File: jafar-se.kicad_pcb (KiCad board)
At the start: 2 copper layers, 33 x 41 mm, 16 parts, among them J1 XBOX LPC, J2 JTAG, J3 D0, J4 PLCC-32 Socket, U1 LC4032V-75TN44I

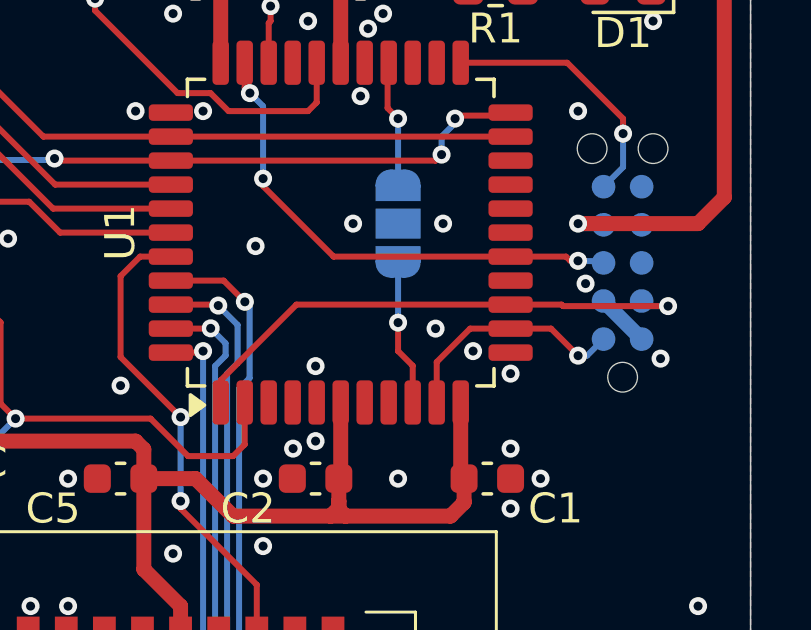
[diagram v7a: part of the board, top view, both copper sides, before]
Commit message: Reroute jtag to not go through CPLD pins
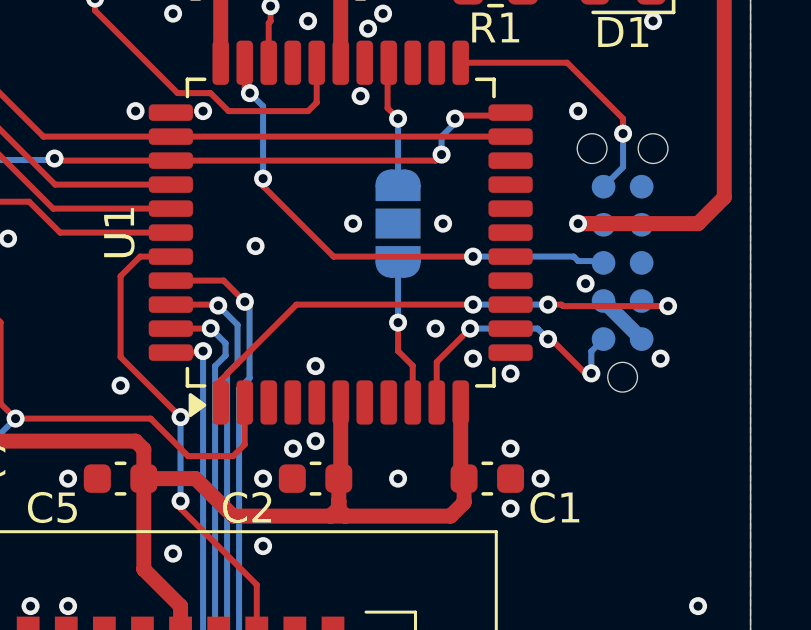
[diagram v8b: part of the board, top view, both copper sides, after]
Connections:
- U1 pad 13: /TCK -> unconnected-(U1-A12-Pad13)
- U1 pad 14: /TDI -> unconnected-(U1-A13-Pad14)
- U1 pad 16: /TDO -> unconnected-(U1-A15-Pad16)
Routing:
- net /TCK: track 7.97 -> 8.89 mm, vias 1 -> 3
- net /TDI: vias 1 -> 3
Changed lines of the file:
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@@
 			(layers "F.Cu" "F.Mask" "F.Paste")
 			(roundrect_rratio 0.25)
-			(net "/TCK")
+			(net "unconnected-(U1-A12-Pad13)")
 			(pinfunction "A12_13")
-			(pintype "bidirectional")
+			(pintype "bidirectional+no_connect")
 		)
 		(pad "14" smd roundrect
@@
 			(layers "F.Cu" "F.Mask" "F.Paste")
 			(roundrect_rratio 0.25)
-			(net "/TDI")
+			(net "unconnected-(U1-A13-Pad14)")
 			(pinfunction "A13_14")
-			(pintype "bidirectional")
+			(pintype "bidirectional+no_connect")
 		)
 		(pad "15" smd roundrect
@@
 			(layers "F.Cu" "F.Mask" "F.Paste")
 			(roundrect_rratio 0.25)
-			(net "/TDO")
+			(net "unconnected-(U1-A15-Pad16)")
 			(pinfunction "A15_16")
-			(pintype "bidirectional")
+			(pintype "bidirectional+no_connect")
 		)
 		(pad "17" smd roundrect
@@
 	)
 	(via
-		(at 143.75 61.75)
+		(at 143.75 62)
 		(size 0.6)
 		(drill 0.3)
@@
 	(segment
 		(start 137.862501 60.2)
-		(end 145 60.2)
+		(end 143.75 60.2)
 		(width 0.2)
 		(layer "F.Cu")
@@
 	)
 	(segment
-		(start 145 60.2)
-		(end 146.7 60.2)
+		(start 135.3375 63.4625)
+		(end 135.3375 62.725001)
 		(width 0.2)
 		(layer "F.Cu")
@@
 	)
 	(segment
-		(start 135.3375 63.4625)
-		(end 135.3375 62.725001)
+		(start 146.25 60.2)
+		(end 146.7 60.2)
 		(width 0.2)
 		(layer "F.Cu")
@@
 	)
 	(via
+		(at 146.25 60.2)
+		(size 0.6)
+		(drill 0.3)
+		(layers "F.Cu" "B.Cu")
+		(net "/TDI")
+	)
+	(via
+		(at 143.75 60.2)
+		(size 0.6)
+		(drill 0.3)
+		(layers "F.Cu" "B.Cu")
+		(net "/TDI")
+	)
+	(via
 		(at 150.25 60.25)
 		(size 0.6)
@@
 	)
 	(segment
+		(start 143.75 60.2)
+		(end 146.25 60.2)
+		(width 0.2)
+		(layer "B.Cu")
+		(net "/TDI")
+	)
+	(segment
 		(start 141.75 63.45)
 		(end 141.7375 63.4625)
@@
 	)
 	(segment
-		(start 143.651471 61)
-		(end 145 61)
+		(start 147.692416 62.492978)
+		(end 147.492978 62.492978)
 		(width 0.2)
 		(layer "F.Cu")
@@
 	)
 	(segment
-		(start 142.5375 63.4625)
-		(end 142.5375 62.113971)
+		(start 146.35 61.35)
+		(end 146.25 61.35)
 		(width 0.2)
 		(layer "F.Cu")
@@
 	)
 	(segment
-		(start 146.348529 61)
-		(end 145 61)
+		(start 142.5375 63.4625)
+		(end 142.5375 62.113971)
 		(width 0.2)
 		(layer "F.Cu")
@@
 	)
 	(segment
-		(start 147.25 61.901471)
-		(end 146.348529 61)
+		(start 147.492978 62.492978)
+		(end 146.35 61.35)
 		(width 0.2)
 		(layer "F.Cu")
@@
 	)
 	(via
-		(at 147.25 61.901471)
+		(at 147.692416 62.492978)
+		(size 0.6)
+		(drill 0.3)
+		(layers "F.Cu" "B.Cu")
+		(net "/TCK")
+	)
+	(via
+		(at 143.651471 61)
+		(size 0.6)
+		(drill 0.3)
+		(layers "F.Cu" "B.Cu")
+		(net "/TCK")
+	)
+	(via
+		(at 146.25 61.35)
 		(size 0.6)
 		(drill 0.3)
@@
 	)
 	(segment
-		(start 147.25 61.901471)
-		(end 147.547529 61.901471)
+		(start 143.651471 61)
+		(end 145.9 61)
 		(width 0.2)
 		(layer "B.Cu")
@@
 	)
 	(segment
-		(start 147.547529 61.901471)
+		(start 147.692416 62.492978)
+		(end 147.692416 61.756584)
+		(width 0.2)
+		(layer "B.Cu")
+		(net "/TCK")
+	)
+	(segment
+		(start 147.692416 61.756584)
 		(end 148.099 61.35)
 		(width 0.2)
@@
 	)
 	(segment
-		(start 139.1 58.6)
-		(end 145 58.6)
+		(start 145.9 61)
+		(end 146.25 61.35)
 		(width 0.2)
-		(layer "F.Cu")
-		(net "/TDO")
+		(layer "B.Cu")
+		(net "/TCK")
 	)
 	(segment
@@
 	)
 	(segment
-		(start 147.247017 58.741051)
-		(end 146.991051 58.741051)
+		(start 143.75 58.6)
+		(end 139.1 58.6)
 		(width 0.2)
 		(layer "F.Cu")
@@
 	)
 	(segment
-		(start 146.85 58.6)
-		(end 145 58.6)
-		(width 0.2)
-		(layer "F.Cu")
-		(net "/TDO")
-	)
-	(segment
-		(start 146.991051 58.741051)
-		(end 146.85 58.6)
-		(width 0.2)
-		(layer "F.Cu")
-		(net "/TDO")
-	)
-	(segment
 		(start 136.1375 52.1375)
 		(end 136.1375 52.976247)
@@
 	)
 	(via
-		(at 147.247017 58.741051)
+		(at 143.75 58.6)
 		(size 0.6)
 		(drill 0.3)
@@
 	)
 	(segment
-		(start 147.247017 58.741051)
-		(end 147.255966 58.75)
+		(start 148.039 58.75)
+		(end 148.099 58.81)
+		(width 0.2)
+		(layer "B.Cu")
+		(net "/TDO")
+	)
+	(segment
+		(start 147.255966 58.75)
+		(end 148.039 58.75)
 		(width 0.2)
 		(layer "B.Cu")
@@
 	)
 	(segment
-		(start 147.255966 58.75)
-		(end 148.039 58.75)
+		(start 147.105966 58.6)
+		(end 147.255966 58.75)
 		(width 0.2)
 		(layer "B.Cu")
@@
 	)
 	(segment
-		(start 148.039 58.75)
-		(end 148.099 58.81)
+		(start 143.75 58.6)
+		(end 147.105966 58.6)
 		(width 0.2)
 		(layer "B.Cu")
